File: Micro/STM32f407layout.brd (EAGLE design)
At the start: 100.1 x 96.7 mm, 68 parts, among them Q1 ASF, Q2 ASV-8, T3 FDN340P, T4 AP1117_LIN_REG

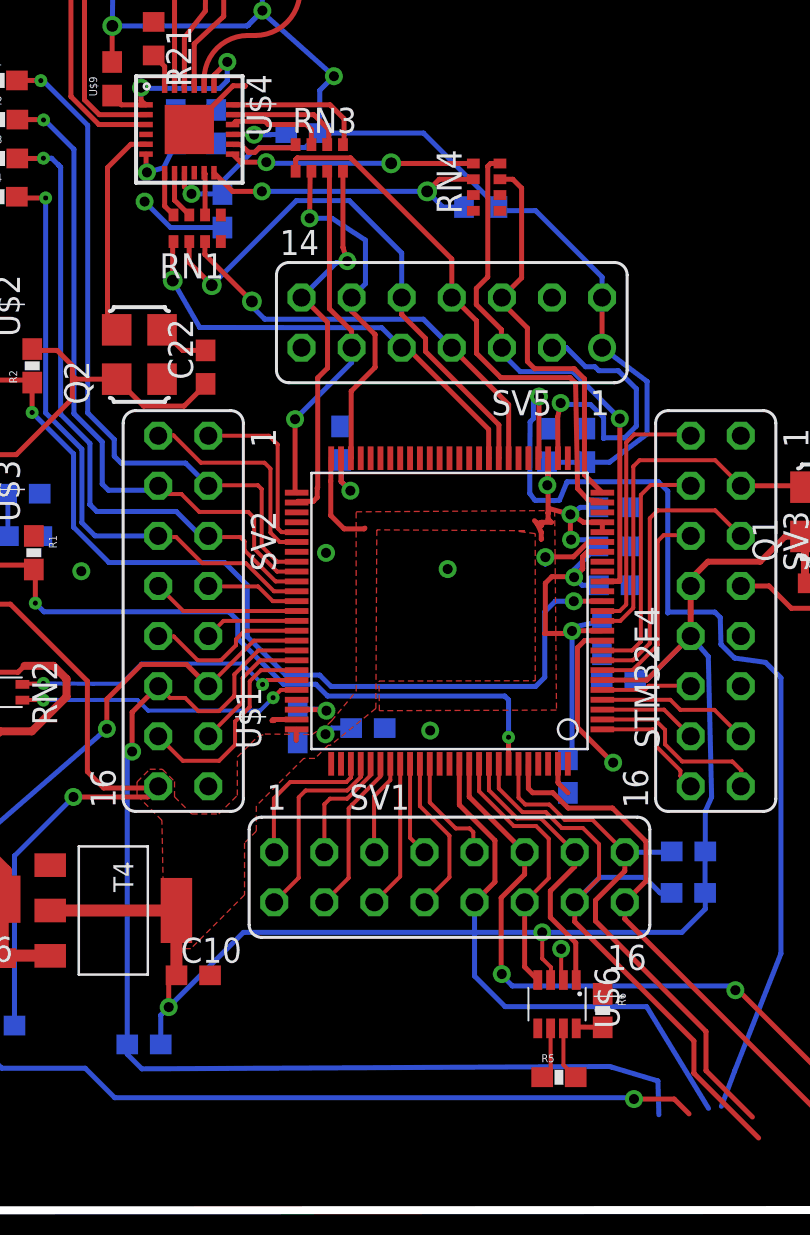
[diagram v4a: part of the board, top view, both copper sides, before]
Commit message: Moved final clearances
Double Checked vias and trace distances
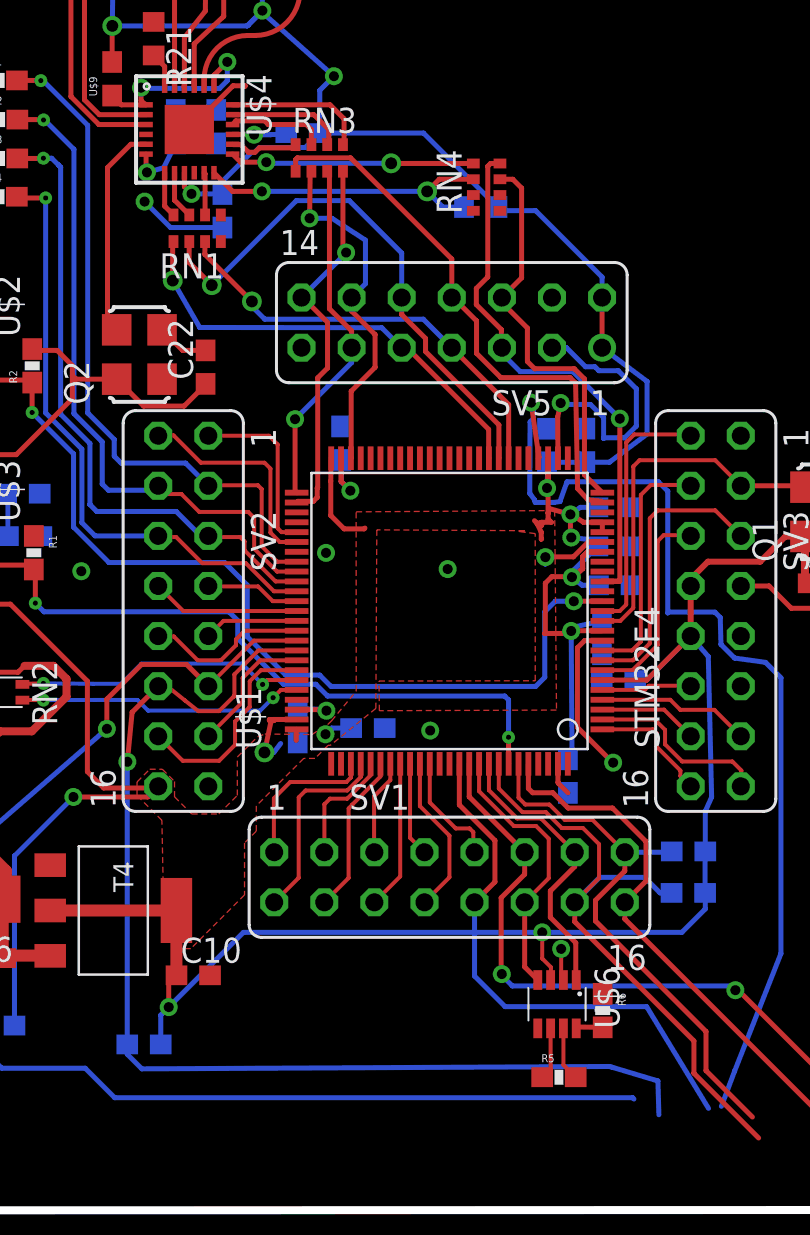
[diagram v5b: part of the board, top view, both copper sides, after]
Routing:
- net GND: track 55.9 -> 60.2 mm, vias 6 -> 7
- net I2C3_SDA: track 69.6 -> 66.5 mm, vias 2 -> 1

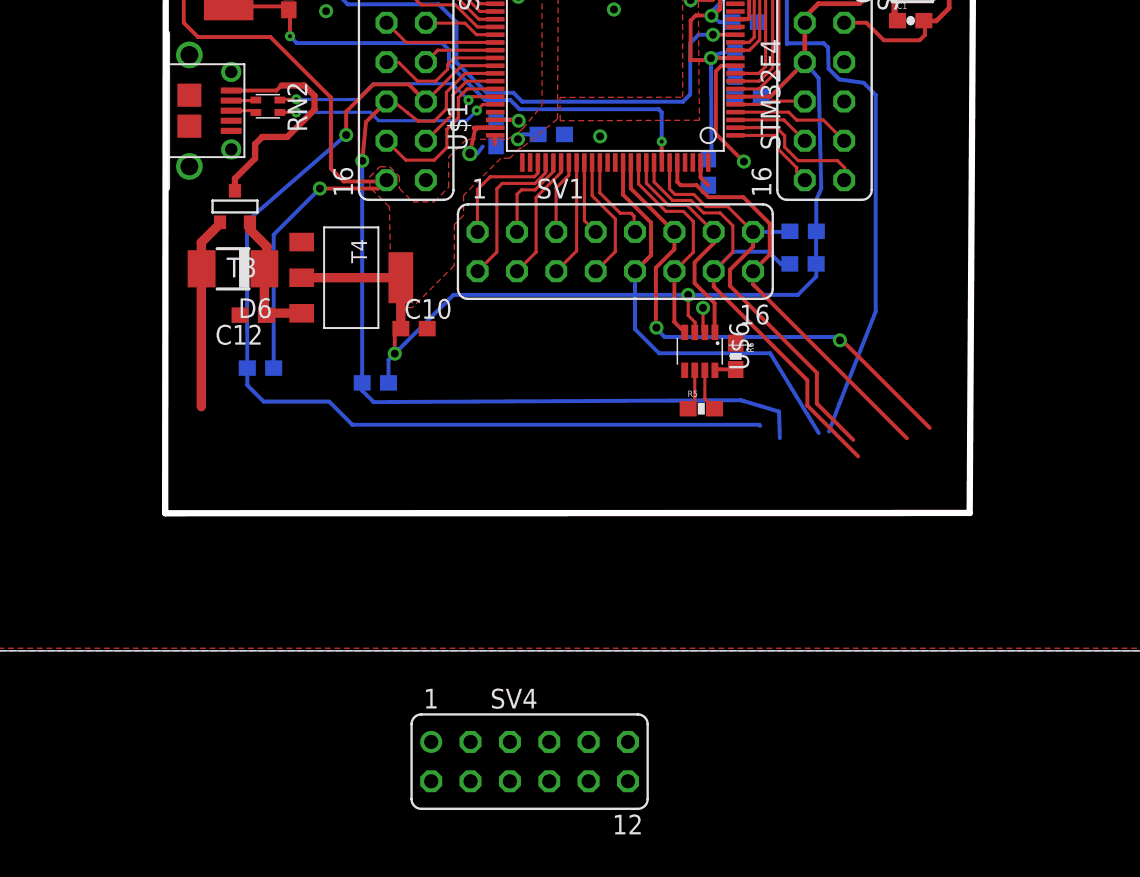
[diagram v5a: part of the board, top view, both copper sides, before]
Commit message: added real header pin
Did a rough draft of connections to backplane
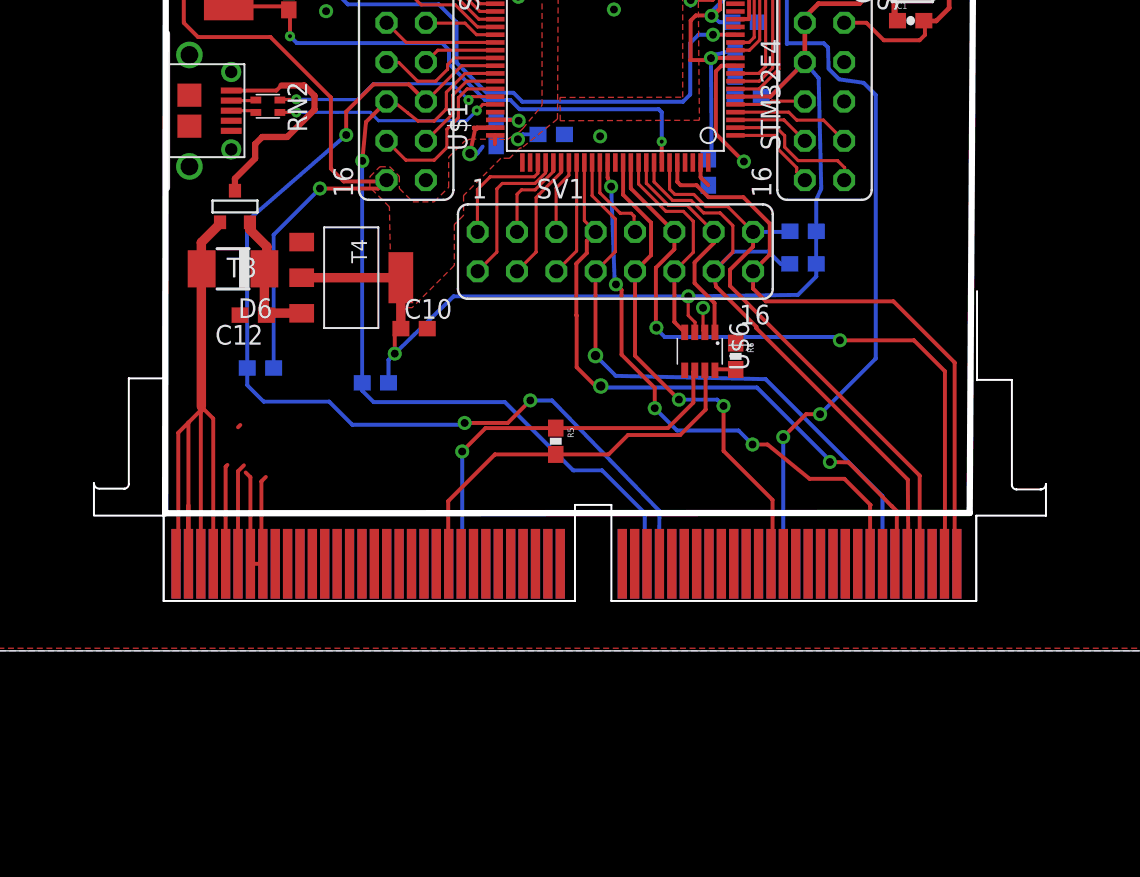
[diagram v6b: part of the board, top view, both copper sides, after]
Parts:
- removed SV4: (no value), con-lsta:FE06-2
- added U$8: HSC8PART-60, Connectors:HSC8-60PINOUUT
- moved R5 9.63 mm to (47.5, 13.5), turned to 270 degrees
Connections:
- removed net PD3: SV1.7, U$1.P84
- removed net PD4: SV1.8, U$1.P85
- removed net PD6: U$1.P87
- new net SHIFTREG_CLK: SV1.8, U$1.P85, U$8.B54
- new net SHIFTREG_DATA: U$1.P87, U$8.T53
- new net SHIFTREG_ENABLE: SV1.7, U$1.P84, U$8.T55
- net +5V: now also U$8.T1, U$8.T2, U$8.T3, U$8.T4; no longer SV4.1
- net ALT_CAMERA_SERVO_MOTOR_PWM: now also U$8.T60; no longer SV4.12
- net CANH1: now also U$8.T23; no longer SV4.3
- net CANL1: now also U$8.B24; no longer SV4.4
- net GND: now also U$8.T5, U$8.T6, U$8.T7, U$8.T8, U$8.T9; no longer SV4.2
- net I2C1_SCL: now also U$8.T57; no longer SV4.5
- net I2C1_SDA: now also U$8.T56; no longer SV4.6
- net I2C3_SCL: now also U$8.B35; no longer SV4.9
- net I2C3_SDA: now also U$8.B36; no longer SV4.10
- net MAIN_CAMERA_SERVO_MOTOR_PWM: now also U$8.T59; no longer SV4.11
- net SONAR_DAC: now also U$8.B46; no longer SV4.8
- net SONAR_PWM: now also U$8.T45; no longer SV4.7
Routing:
- net +5V: track 12.4 -> 56.6 mm
- net SHIFTREG_ENABLE: track 0.00 -> 42.1 mm, vias 0 -> 2
- net SHIFTREG_CLK: track 0.00 -> 40.2 mm, vias 0 -> 1
- net SHIFTREG_DATA: track 0.00 -> 37.2 mm, vias 0 -> 4
- net GND: track 60.2 -> 85.9 mm
- net CANL1: track 2.66 -> 25.6 mm, vias 0 -> 1
- net CANH1: track 2.74 -> 25.7 mm
- net ALT_CAMERA_SERVO_MOTOR_PWM: track 26.7 -> 41.0 mm
- net MAIN_CAMERA_SERVO_MOTOR_PWM: track 32.7 -> 44.6 mm
- net SONAR_DAC: track 52.1 -> 63.1 mm, vias 1 -> 3
- net I2C1_SCL: track 28.0 -> 37.8 mm
- net I2C1_SDA: track 32.5 -> 40.8 mm
- net PD4: track 8.17 -> 0.00 mm
- net SONAR_PWM: track 27.3 -> 32.2 mm, vias 0 -> 2
- net PD3: track 4.78 -> 0.00 mm
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
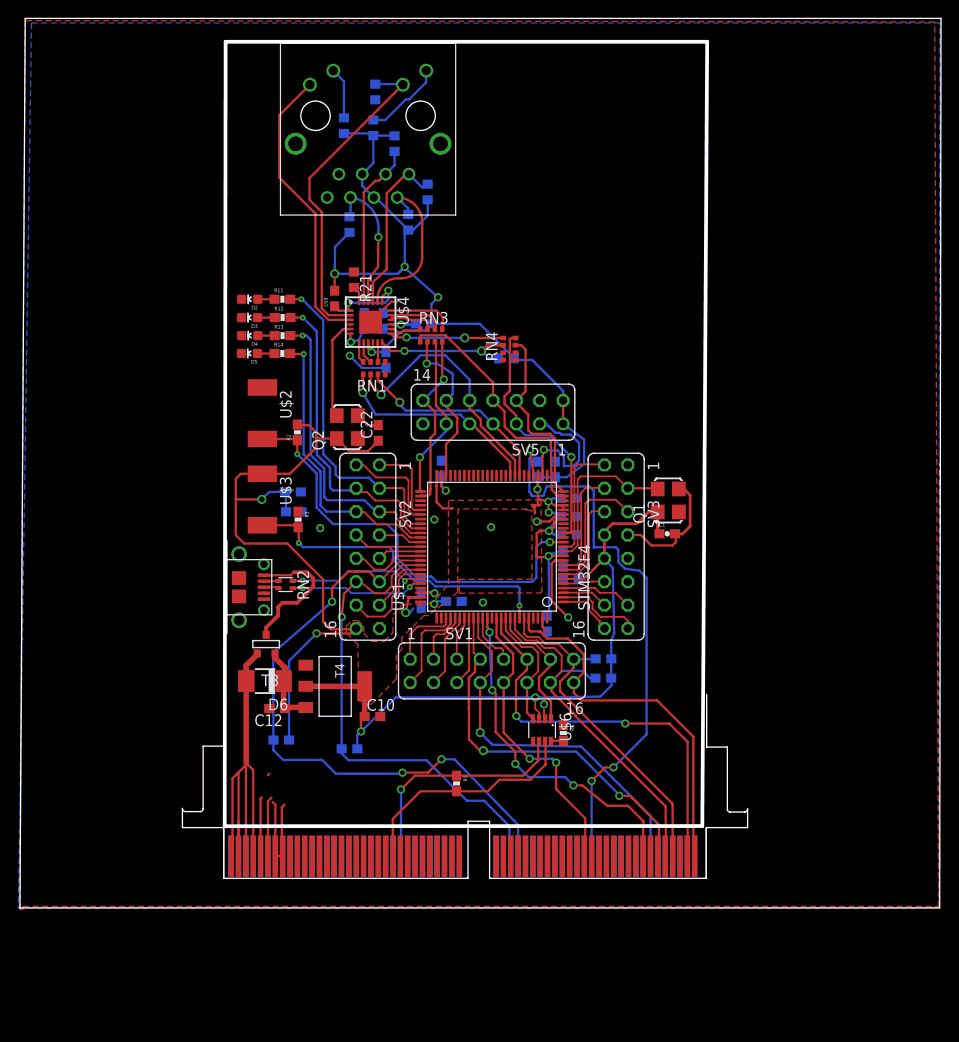
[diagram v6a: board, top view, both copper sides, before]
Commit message: Imprved spacing, changed bottom pinouts
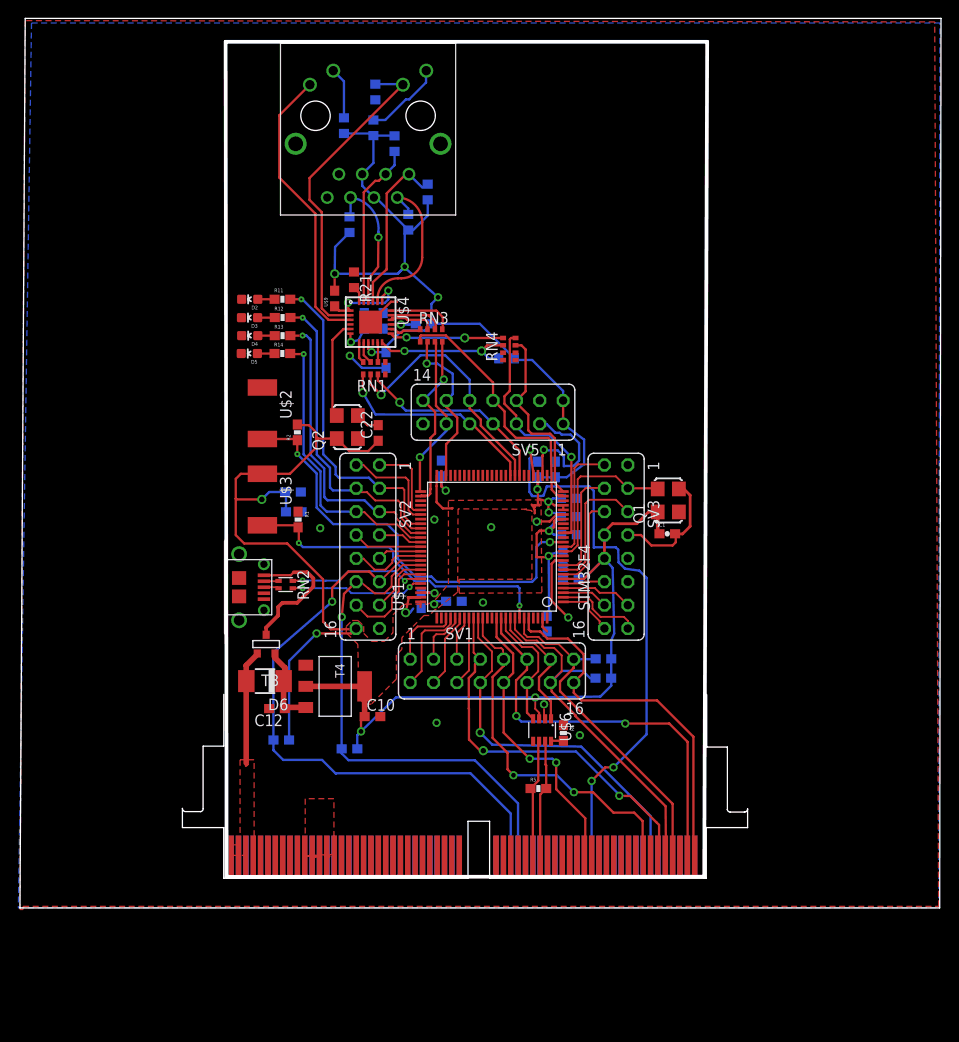
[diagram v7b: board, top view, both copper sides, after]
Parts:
- moved R5 8.91 mm to (56.4, 13.0), turned to 0 degrees
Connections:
- removed net PD5: SV1.9, U$1.P86
- new net PD6: U$1.P87
- net CANH1: now also U$8.T39; no longer U$8.T23
- net CANL1: now also U$8.T38; no longer U$8.B24
- net GND: now also U$8.T11, U$8.T12, U$8.T13, U$8.T14, U$8.T15; no longer U$8.T5, U$8.T6, U$8.T7, U$8.T8, U$8.T9
- net I2C3_SCL: now also U$8.B36; no longer U$8.B35
- net I2C3_SDA: now also U$8.B35; no longer U$8.B36
- net SHIFTREG_DATA: now also SV1.9, U$1.P86; no longer U$1.P87
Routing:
- net +5V: track 56.6 -> 13.1 mm
- net GND: track 85.9 -> 62.4 mm, vias 7 -> 9
- net CANH1: track 25.7 -> 12.8 mm
- net CANL1: track 25.6 -> 13.0 mm, vias 1 -> 0
- net PD5: track 5.83 -> 0.00 mm
- net SHIFTREG_DATA: track 37.2 -> 39.8 mm, vias 4 -> 2
- net I2C3_SCL: track 54.0 -> 56.6 mm
- net I2C3_SDA: track 67.1 -> 65.7 mm, vias 3 -> 1
- added copper zone on layer 1, net +5V
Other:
- outline, holes or cut-outs redrawn

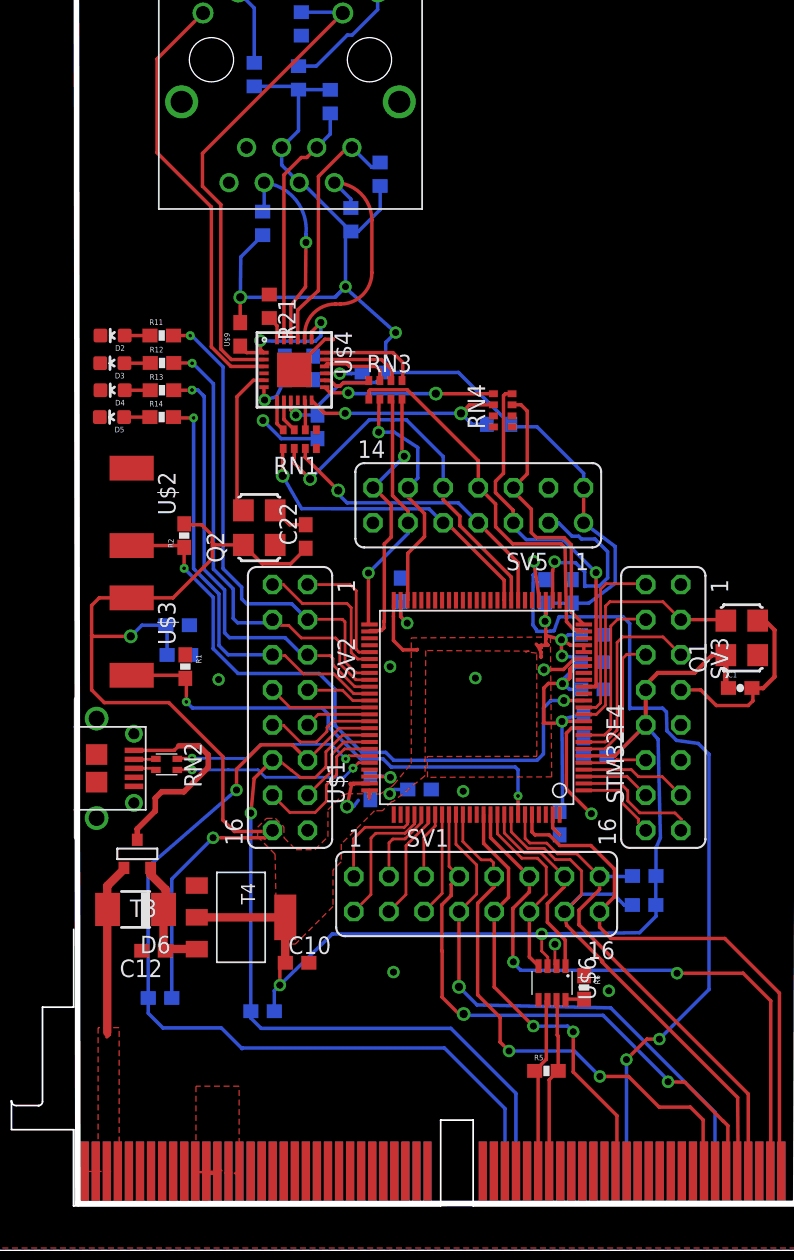
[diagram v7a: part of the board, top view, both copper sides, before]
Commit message: Fixed DRC Errors, Began fixing other problems
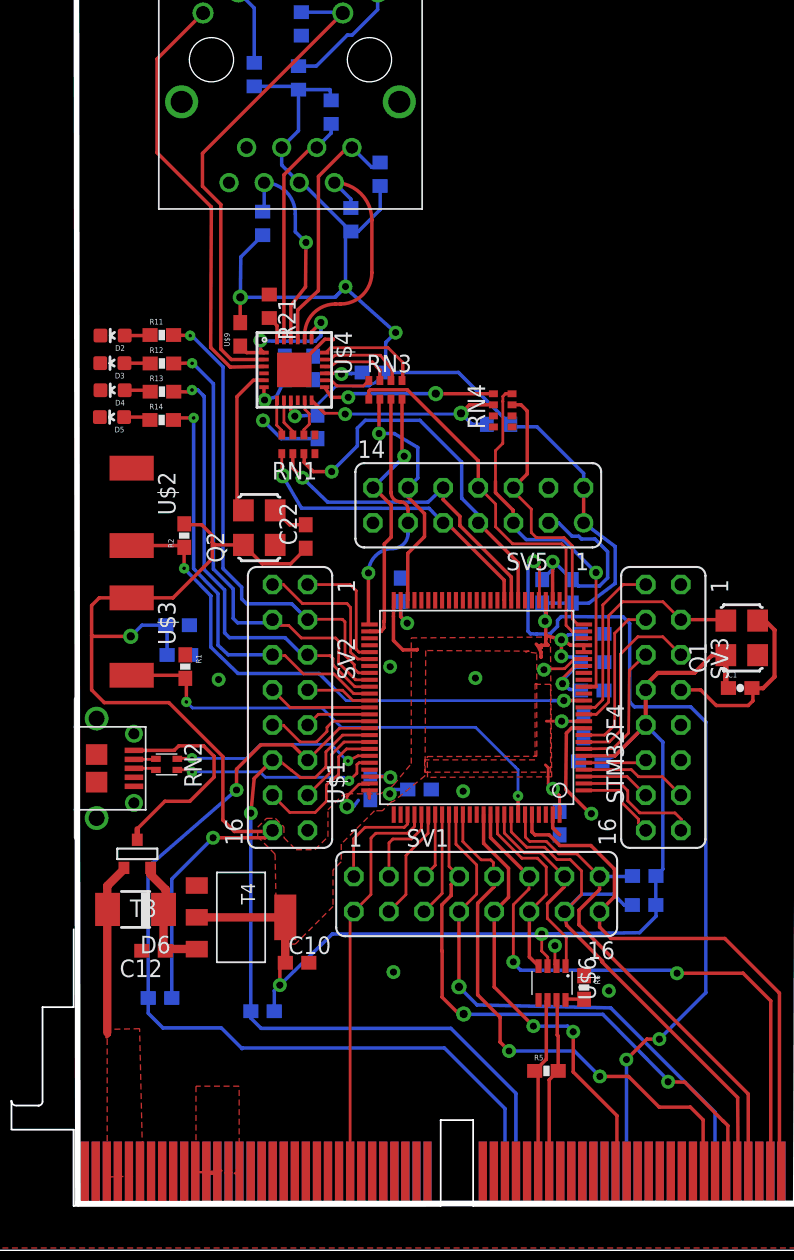
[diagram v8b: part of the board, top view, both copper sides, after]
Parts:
- moved R16 0.77 mm to (40.8, 82.3)
- moved C18 0.53 mm to (59.5, 35.4)
- moved RN1 0.39 mm to (38.4, 58.3)
- moved R14 0.21 mm to (28.5, 60.1)
- moved C4 0.20 mm to (56.1, 47.7)
- moved R13 0.10 mm to (28.6, 62.1)
- moved C11 0.08 mm to (59.7, 40.5)
- moved C17 0.06 mm to (59.7, 44.6)
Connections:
- removed net PC11: SV1.2, U$1.P79
- new net TEMP_BACKUP: SV1.2, U$1.P79, U$8.T25
- net +5V: now also U$8.T5, U$8.T6; no longer U$8.T1, U$8.T2
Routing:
- net TEMP_BACKUP: track 0.00 -> 29.2 mm
- net PC11: track 10.1 -> 0.00 mm
- net N$4: track 47.6 -> 41.4 mm
- net CRS_DV: track 22.1 -> 27.8 mm
- net +3V3: track 294.6 -> 288.8 mm, vias 14 -> 15
- net RXD0: track 27.8 -> 23.5 mm
- net SONAR_DAC: track 63.1 -> 64.0 mm
- net GND: track 62.4 -> 61.6 mm
- net PH1: track 13.1 -> 12.3 mm
- net RD+: track 18.0 -> 17.2 mm
- net N$9: track 2.16 -> 2.89 mm
- net N$57: track 15.0 -> 15.6 mm
- net PC13: track 10.4 -> 9.87 mm
- net USB_D+: track 14.6 -> 15.1 mm
- net OSC_IN: track 18.4 -> 17.9 mm
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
